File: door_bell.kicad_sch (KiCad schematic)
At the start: 77 parts, among them J1 8-10V AC/DC, J2 Speaker, J3 SWITCH1, J4 UART, J5 MicroSD, J6 Door panel, K1 HJR 1-2C, Q1 BC847, SW1 Reset, SW2 Boot, U1 NCP1117-5v, U2 MAX98357A, U3 NCP1117-3v3, U4 DS3231M, U5 MAX3232, U6 ESP32-WROVER-B, U7 74LVC2G14

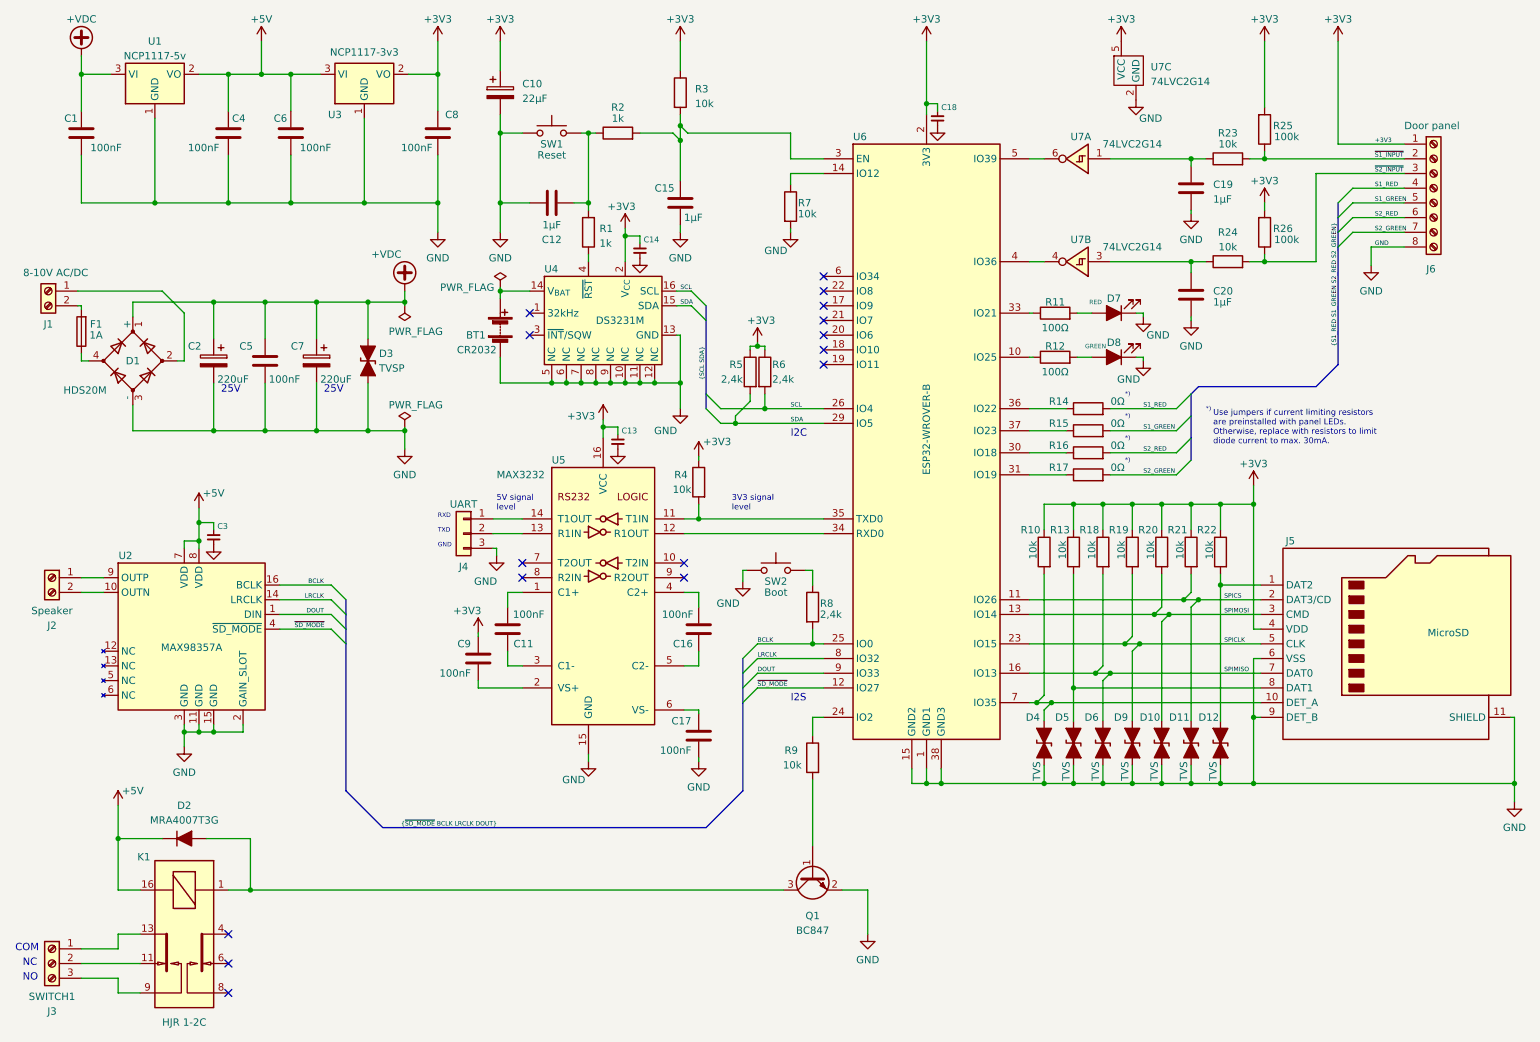
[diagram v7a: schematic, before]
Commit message: Change from IO2 to IO12 for relay
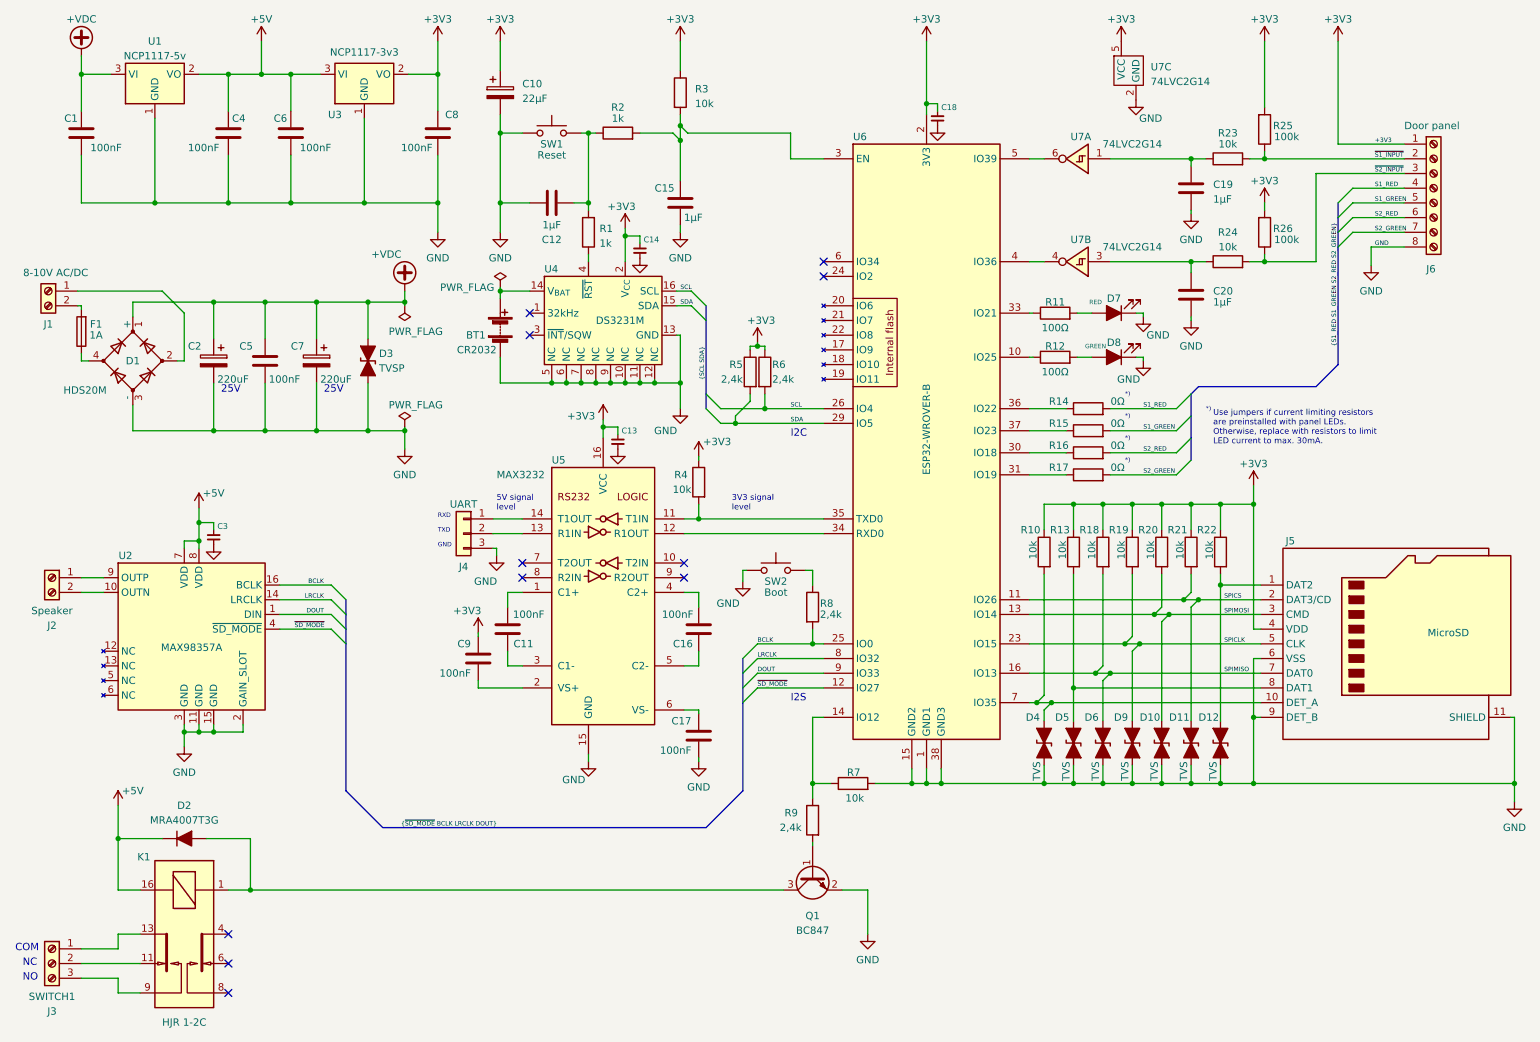
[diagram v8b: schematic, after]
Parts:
- R9: value 10k -> 2,4k
- U2: footprint Package_DFN_QFN:TQFN-24-1EP_4x4mm_P0.5mm_EP2.6x2.6mm -> Package_DFN_QFN_espena:TQFN-16-1EP_3x3mm_P0.5mm_EP1.23x1.23mm
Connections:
- net at R7.1, U6.14 (IO12): now also R9.1
- net at U6.24 (IO2): no longer R9.1
- no-connect marks 16 -> 11
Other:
- note added: "Use jumpers if current limiting resistors are preinstalled with panel LEDs. Otherwise, replace with resistors to limit LED current to max. 30mA."
- note removed: "Use jumpers if current limiting resistors are preinstalled with panel LEDs. Otherwise, replace with resistors to limit diode current to max. 30mA."
- moved on the sheet: R7, R9
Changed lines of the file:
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@@
   (junction (at 86.36 67.945) (diameter 0) (color 0 0 0 0)
   )
+  (junction (at 173.99 151.13) (diameter 0) (color 0 0 0 0)
+  )
   (junction (at 278.13 151.13) (diameter 0) (color 0 0 0 0)
   )
@@
   (junction (at 111.76 81.915) (diameter 0) (color 0 0 0 0)
   )
+  (junction (at 156.845 151.13) (diameter 0) (color 0 0 0 0)
+  )
   (junction (at 212.09 151.13) (diameter 0) (color 0 0 0 0)
   )
@@
   (junction (at 222.25 60.96) (diameter 0) (color 0 0 0 0)
   )
-  (no_connect (at 158.75 78.74))
-  (no_connect (at 158.75 71.12))
   (no_connect (at 158.75 63.5))
   (no_connect (at 107.95 73.66))
@@
   (no_connect (at 106.68 115.57))
   (no_connect (at 107.95 69.85))
-  (no_connect (at 158.75 73.66))
-  (no_connect (at 158.75 66.04))
+  (no_connect (at 158.75 60.96))
   (no_connect (at 55.88 177.165))
   (no_connect (at 55.88 182.245))
-  (no_connect (at 158.75 68.58))
   (no_connect (at 106.68 113.03))
   (no_connect (at 134.62 115.57))
-  (no_connect (at 158.75 76.2))
   (bus_entry (at 247.65 53.34) (size 2.54 -2.54)
     (stroke (width 0) (type default))
@@
     (stroke (width 0) (type default))
   )
+  (wire (pts (xy 167.64 151.13) (xy 173.99 151.13))
+    (stroke (width 0) (type default))
+  )
   (wire (pts (xy 99.06 133.35) (xy 99.06 134.62))
     (stroke (width 0) (type default))
@@
     (stroke (width 0) (type default))
   )
-  (wire (pts (xy 156.845 139.7) (xy 156.845 142.875))
+  (wire (pts (xy 156.845 139.7) (xy 156.845 151.13))
     (stroke (width 0) (type default))
   )
@@
     (stroke (width 0) (type default))
   )
-  (wire (pts (xy 156.845 150.495) (xy 156.845 161.925))
+  (wire (pts (xy 156.845 161.29) (xy 156.845 161.925))
     (stroke (width 0) (type default))
   )
@@
     (stroke (width 0) (type default))
   )
-  (wire (pts (xy 153.035 45.72) (xy 158.75 45.72))
-    (stroke (width 0) (type default))
-  )
   (wire (pts (xy 133.985 54.61) (xy 133.985 55.88))
     (stroke (width 0) (type default))
@@
     (stroke (width 0) (type default))
   )
-  (wire (pts (xy 153.035 45.72) (xy 153.035 47.625))
-    (stroke (width 0) (type default))
-  )
   (wire (pts (xy 198.12 137.16) (xy 234.315 137.16))
     (stroke (width 0) (type default))
@@
     (stroke (width 0) (type default))
   )
-  (wire (pts (xy 153.035 55.245) (xy 153.035 55.88))
-    (stroke (width 0) (type default))
-  )
   (wire (pts (xy 212.09 128.27) (xy 213.36 127))
     (stroke (width 0) (type default))
@@
     (stroke (width 0) (type default))
   )
+  (wire (pts (xy 156.845 151.13) (xy 156.845 153.67))
+    (stroke (width 0) (type default))
+  )
   (wire (pts (xy 30.48 42.545) (xy 30.48 50.8))
     (stroke (width 0) (type default))
@@
     (stroke (width 0) (type default))
   )
+  (wire (pts (xy 156.845 151.13) (xy 160.02 151.13))
+    (stroke (width 0) (type default))
+  )
   (bus (pts (xy 138.43 71.12) (xy 138.43 83.82))
     (stroke (width 0) (type default))
@@
     (effects (font (size 1.27 1.27)) (justify left bottom))
   )
-  (text "Use jumpers if current limiting resistors\nare preinstalled with panel LEDs.\nOtherwise, replace with resistors to limit\ndiode current to max. 30mA."
+  (text "Use jumpers if current limiting resistors\nare preinstalled with panel LEDs.\nOtherwise, replace with resistors to limit\nLED current to max. 30mA."
     (at 226.06 92.71 0)
     (effects (font (size 1.016 1.016)) (justify left bottom))
@@
     )
   )
-  (symbol (lib_id "power:GND") (at 153.035 55.88 0) (unit 1)
-    (in_bom yes) (on_board yes) (dnp no)
-    (property "Reference" "#PWR027" (at 153.035 62.23 0)
-      (effects (font (size 1.27 1.27)) hide)
-    )
-    (property "Value" "GND" (at 150.495 59.055 0)
-      (effects (font (size 1.27 1.27)))
-    )
-    (property "Footprint" "" (at 153.035 55.88 0)
-      (effects (font (size 1.27 1.27)) hide)
-    )
-    (property "Datasheet" "" (at 153.035 55.88 0)
-      (effects (font (size 1.27 1.27)) hide)
-    )
-    (pin "1")
-    (instances
-      (project "door_bell"
-        (path "/c78ad4c4-54c1-4b1d-a971-e4b8abed6bf8"
-          (reference "#PWR027") (unit 1)
-        )
-      )
-    )
-  )
   (symbol (lib_id "Device:Battery") (at 102.87 72.39 0) (unit 1)
     (in_bom yes) (on_board yes) (dnp no)
@@
     )
   )
-  (symbol (lib_id "Device:R") (at 153.035 51.435 0) (unit 1)
+  (symbol (lib_id "Device:R") (at 163.83 151.13 90) (unit 1)
     (in_bom yes) (on_board yes) (dnp no)
-    (property "Reference" "R7" (at 154.305 50.8 0)
+    (property "Reference" "R7" (at 165.1 149.225 90)
       (effects (font (size 1.27 1.27)) (justify left))
     )
-    (property "Value" "10k" (at 154.305 52.705 0)
+    (property "Value" "10k" (at 165.735 153.67 90)
       (effects (font (size 1.27 1.27)) (justify left))
     )
-    (property "Footprint" "Resistor_SMD:R_0805_2012Metric_Pad1.20x1.40mm_HandSolder" (at 151.257 51.435 90)
+    (property "Footprint" "Resistor_SMD:R_0805_2012Metric_Pad1.20x1.40mm_HandSolder" (at 163.83 152.908 90)
       (effects (font (size 1.27 1.27)) hide)
     )
-    (property "Datasheet" "~" (at 153.035 51.435 0)
+    (property "Datasheet" "~" (at 163.83 151.13 0)
       (effects (font (size 1.27 1.27)) hide)
     )
@@
       (effects (font (size 1.27 1.27)))
     )
-    (property "Footprint" "Package_DFN_QFN:TQFN-24-1EP_4x4mm_P0.5mm_EP2.6x2.6mm" (at 49.53 161.29 0)
+    (property "Footprint" "Package_DFN_QFN_espena:TQFN-16-1EP_3x3mm_P0.5mm_EP1.23x1.23mm" (at 49.53 161.29 0)
       (effects (font (size 1.27 1.27)) hide)
     )
@@
     )
   )
-  (symbol (lib_id "Device:R") (at 156.845 146.685 0) (mirror y) (unit 1)
+  (symbol (lib_id "Device:R") (at 156.845 157.48 0) (mirror y) (unit 1)
     (in_bom yes) (on_board yes) (dnp no)
-    (property "Reference" "R9" (at 154.305 145.415 0)
+    (property "Reference" "R9" (at 154.305 156.21 0)
       (effects (font (size 1.27 1.27)) (justify left))
     )
-    (property "Value" "10k" (at 154.94 147.955 0)
+    (property "Value" "2,4k" (at 154.94 158.75 0)
       (effects (font (size 1.27 1.27)) (justify left))
     )
-    (property "Footprint" "Resistor_SMD:R_0805_2012Metric_Pad1.20x1.40mm_HandSolder" (at 158.623 146.685 90)
+    (property "Footprint" "Resistor_SMD:R_0805_2012Metric_Pad1.20x1.40mm_HandSolder" (at 158.623 157.48 90)
       (effects (font (size 1.27 1.27)) hide)
     )
-    (property "Datasheet" "~" (at 156.845 146.685 0)
+    (property "Datasheet" "~" (at 156.845 157.48 0)
       (effects (font (size 1.27 1.27)) hide)
     )
